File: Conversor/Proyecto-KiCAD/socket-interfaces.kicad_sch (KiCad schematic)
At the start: 24 parts, among them J7 DIMM100, P10 Header PWM, P11 Header ADC, P12 Header GPIO, P13 Header SD, P7 Header 7X2, P8 Header UART, P9 Header I2C, SW1 Switch, SW2 Switch, SW3 Switch, SW4 Switch

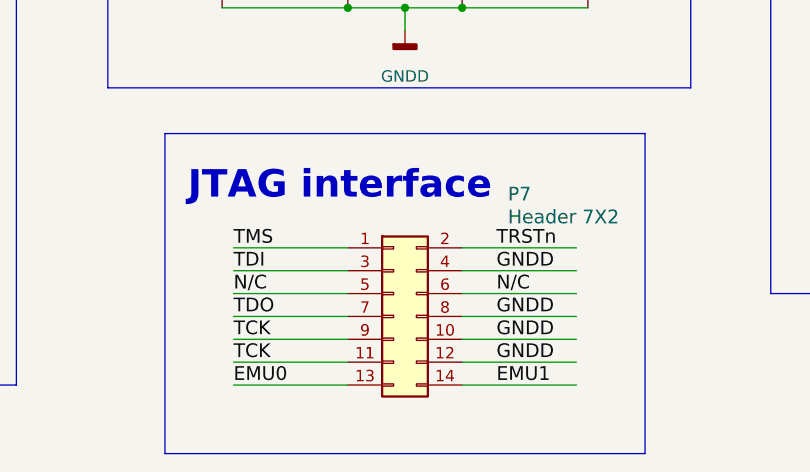
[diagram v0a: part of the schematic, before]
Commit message: Solucionar la union de las lineas de datos I2C
- Segun una evaluation board de Texas, si ya estan separadas las lineas
de I2C como en este caso, solo hay que agregar un adaptador de push-pull
a opne-drain a la salida del aislador
- Se mandó el mail a MayerPCB
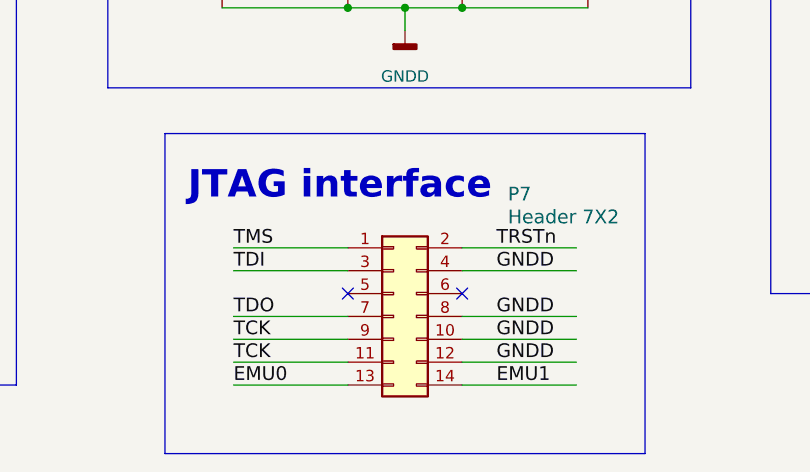
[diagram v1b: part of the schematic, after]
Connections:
- net N/C: no longer names the net of P7.6 (Pin_6)
- net N/C: no longer names the net of P7.5 (Pin_5)
- no-connect marks 15 -> 17
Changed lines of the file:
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@@
   (no_connect (at 35.56 29.21))
   (no_connect (at 60.96 34.29))
+  (no_connect (at 133.35 154.94))
+  (no_connect (at 120.65 154.94))
   (no_connect (at 60.96 67.31))
   (no_connect (at 60.96 31.75))
@@
     (stroke (width 0) (type default) (color 0 0 0 0))
   )
-  (wire (pts (xy 107.95 154.94) (xy 120.65 154.94))
-    (stroke (width 0) (type default) (color 0 0 0 0))
-  )
   (wire (pts (xy 25.4 74.93) (xy 35.56 74.93))
     (stroke (width 0) (type default) (color 0 0 0 0))
@@
   )
   (wire (pts (xy 120.65 90.17) (xy 120.65 93.98))
-    (stroke (width 0) (type default) (color 0 0 0 0))
-  )
-  (wire (pts (xy 146.05 154.94) (xy 133.35 154.94))
     (stroke (width 0) (type default) (color 0 0 0 0))
   )
@@
     (effects (font (size 1.27 1.27)) (justify left bottom))
   )
-  (label "N/C" (at 137.16 154.94 0)
-    (effects (font (size 1.524 1.524)) (justify left bottom))
-  )
   (label "GPIO-12" (at 25.4 110.49 0)
     (effects (font (size 1.524 1.524)) (justify left bottom))
@@
     (effects (font (size 1.524 1.524)) (justify left bottom))
   )
-  (label "N{slash}C" (at 107.95 154.94 0)
-    (effects (font (size 1.524 1.524)) (justify left bottom))
-  )

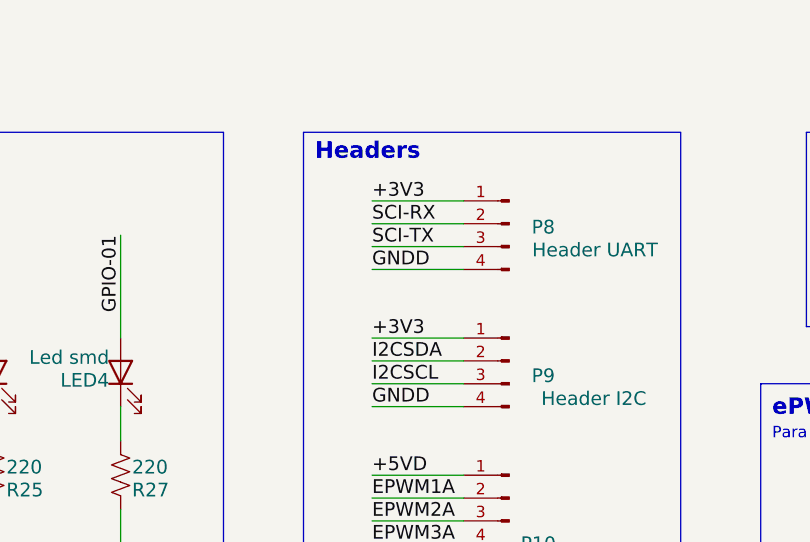
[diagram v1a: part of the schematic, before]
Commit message: Agregar resistencias de pull-up faltantes
- Agregar resistencias de pull-up a la salida de cada inversor del
74LS06
- Crear plano de U5V en la capa superior alrededor del FTDI
- Ponerle los valores a los componentes para poder generar correctamente
el BOM (Bill of Materials)
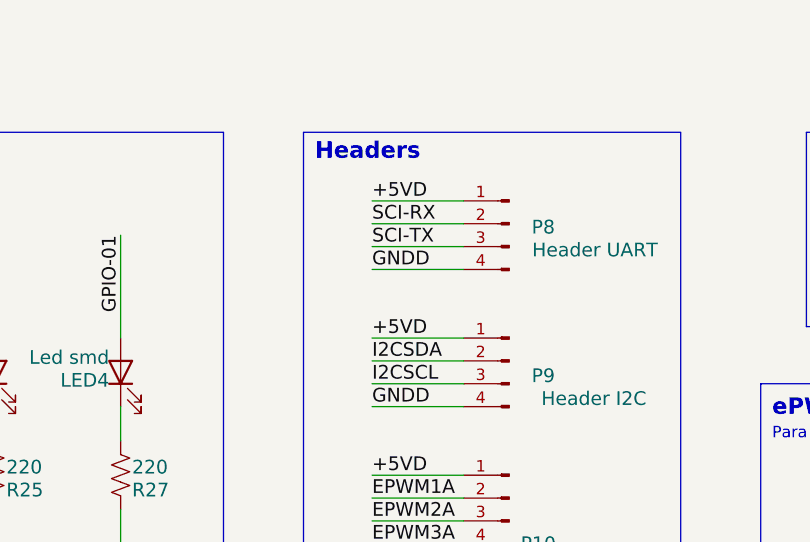
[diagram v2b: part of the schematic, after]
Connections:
- net +3V3: no longer P8.1 (Pin_1), P9.1 (Pin_1)
- net +5VD: now also P8.1 (Pin_1), P9.1 (Pin_1)
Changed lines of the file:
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@@
     (effects (font (size 1.524 1.524)) (justify left bottom))
   )
-  (label "+3V3" (at 175.26 35.56 0)
+  (label "+5VD" (at 175.26 35.56 0)
     (effects (font (size 1.524 1.524)) (justify left bottom))
   )
@@
     (effects (font (size 1.524 1.524)) (justify left bottom))
   )
-  (label "+3V3" (at 175.26 50.8 0)
+  (label "+5VD" (at 175.26 50.8 0)
     (effects (font (size 1.524 1.524)) (justify left bottom))
   )

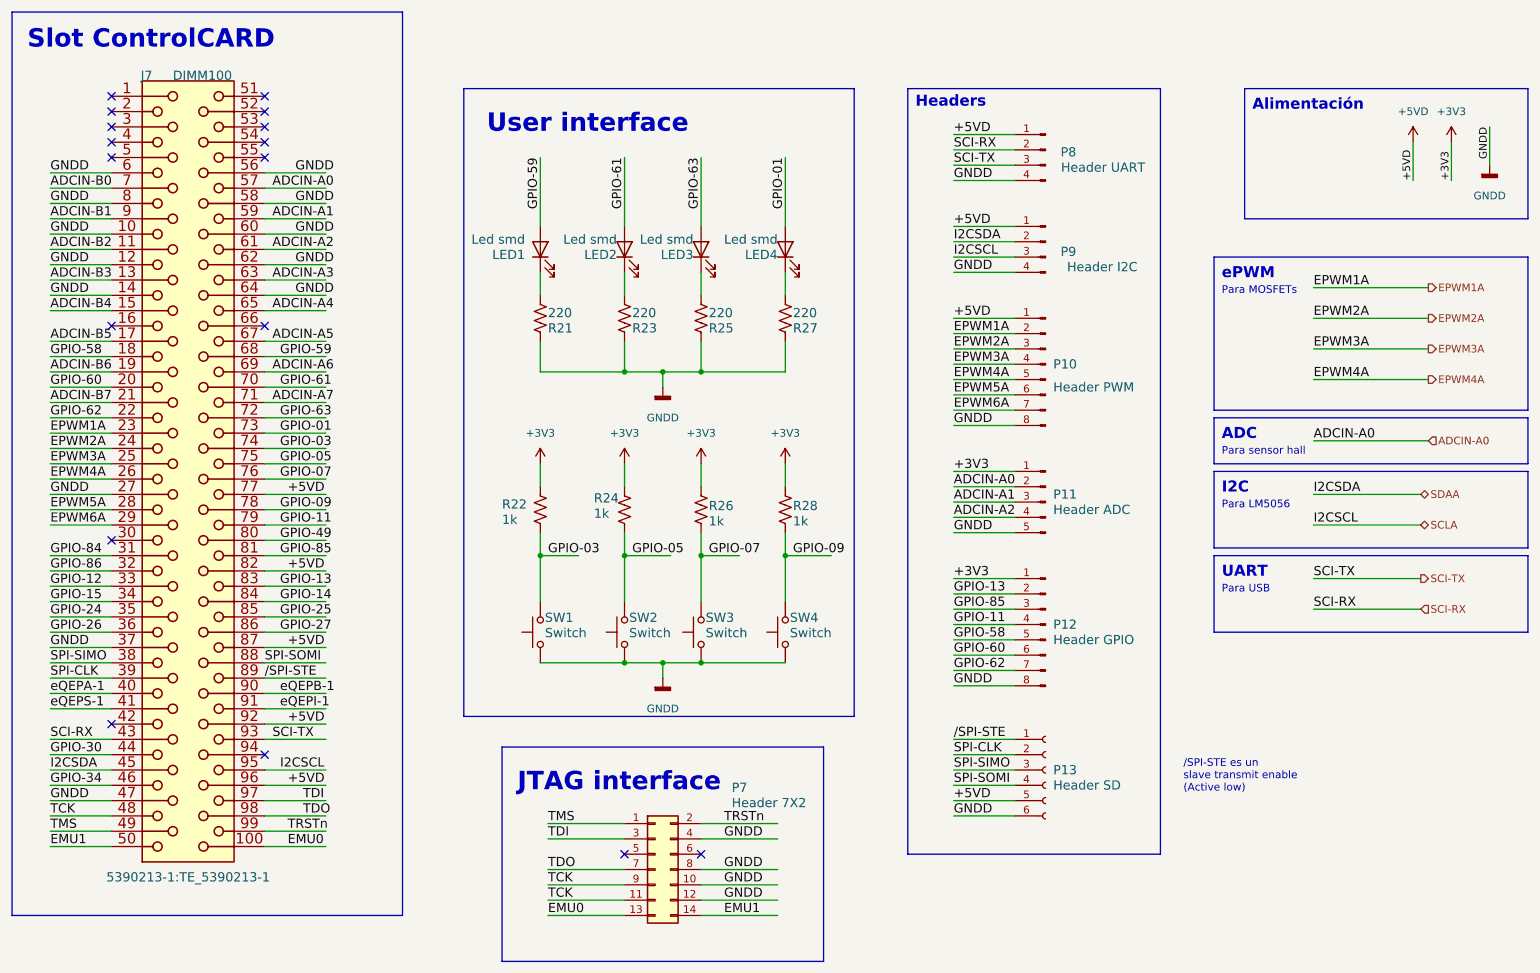
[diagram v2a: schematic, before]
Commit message: Eliminar resistencias de pull-up de SCL y SDAI
- Se pueden remover las Rpu del lado del sensor ya que las Rpu de esas
lineas estan del otro lado (la barrera de aislación proteje de daños).
La de SDAO tiene que quedar por la salida open-drain del LM5056.
- También cambiar las Rpu de 10k a 4k7, porque la capacidad del bus es
muy baja (un solo esclavo y pistas cortas). Así se disminuye es rise
time (Rpu*Cbus) a la mitad.
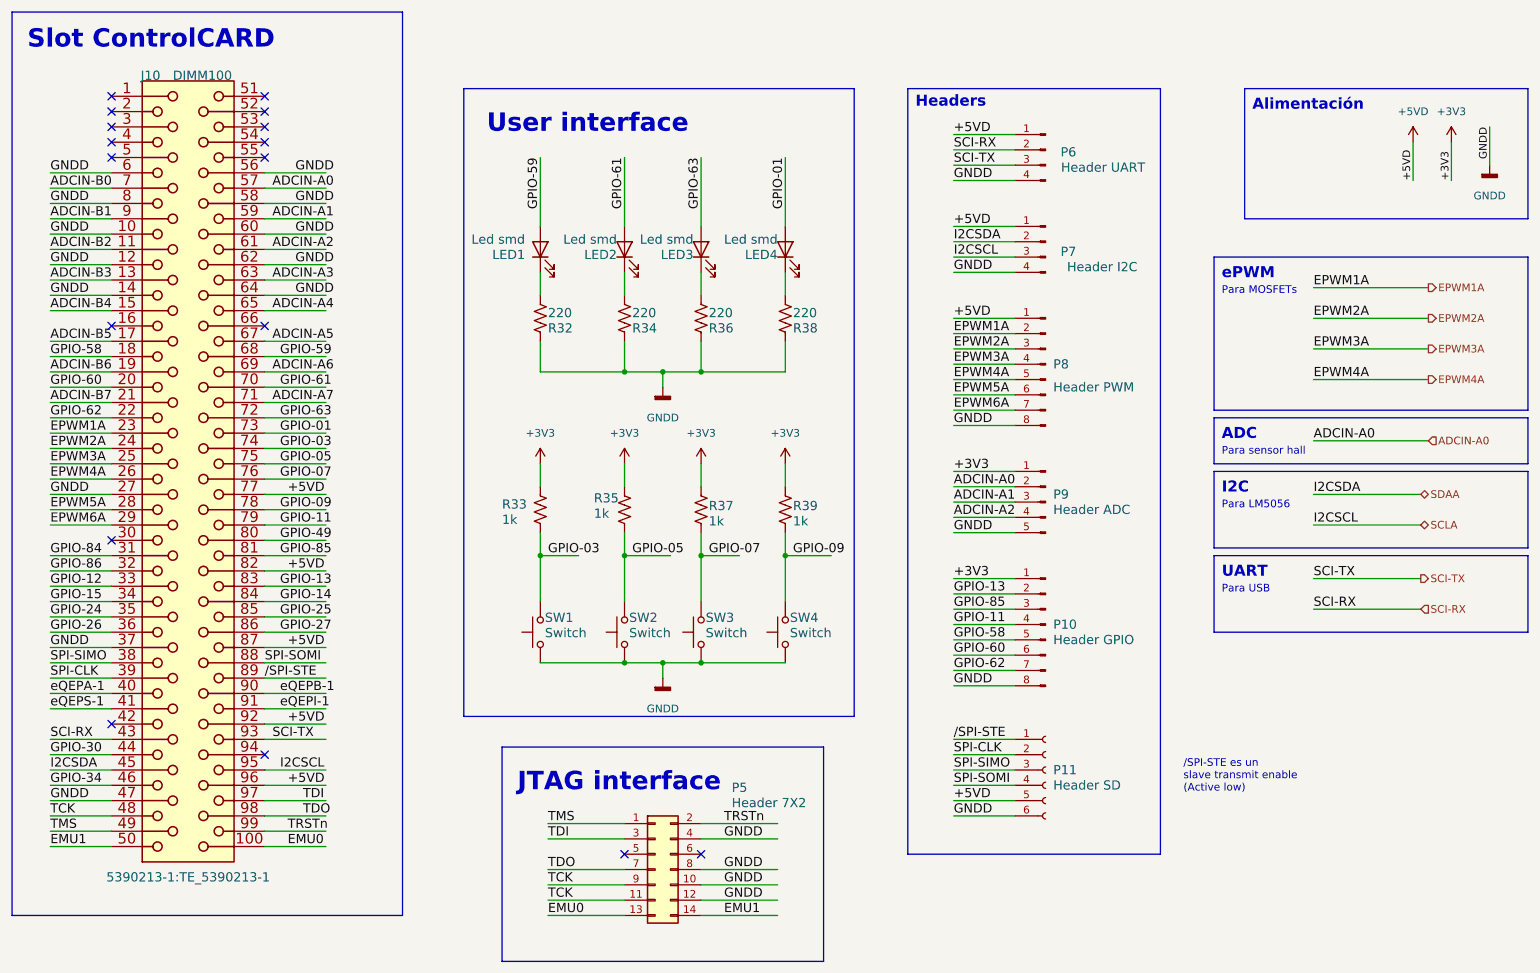
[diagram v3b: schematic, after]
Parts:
- renumbered J7 to J10, P12 to P10, P13 to P11, P7 to P5, P8 to P6, P9 to P7, P10 to P8, P11 to P9, R21 to R32, R22 to R33, R23 to R34, R24 to R35, R25 to R36, R26 to R37, R27 to R38, R28 to R39
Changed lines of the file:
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@@
   (symbol (lib_id "power:+3V3") (at 133.35 90.17 0) (unit 1)
     (in_bom yes) (on_board yes) (fields_autoplaced)
-    (property "Reference" "#PWR080" (id 0) (at 133.35 93.98 0)
+    (property "Reference" "#PWR088" (id 0) (at 133.35 93.98 0)
       (effects (font (size 1.27 1.27)) hide)
     )
@@
   (symbol (lib_id "Device:R_US") (at 133.35 97.79 180) (unit 1)
     (in_bom yes) (on_board yes)
-    (property "Reference" "R26" (id 0) (at 134.62 98.044 0)
+    (property "Reference" "R37" (id 0) (at 134.62 98.044 0)
       (effects (font (size 1.524 1.524)) (justify right top))
     )
@@
   (symbol (lib_id "power:+3V3") (at 120.65 90.17 0) (unit 1)
     (in_bom yes) (on_board yes) (fields_autoplaced)
-    (property "Reference" "#PWR077" (id 0) (at 120.65 93.98 0)
+    (property "Reference" "#PWR085" (id 0) (at 120.65 93.98 0)
       (effects (font (size 1.27 1.27)) hide)
     )
@@
   (symbol (lib_id "Connector:Conn_01x04_Male") (at 190.5 38.1 0) (mirror y) (unit 1)
     (in_bom yes) (on_board yes)
-    (property "Reference" "P8" (id 0) (at 195.58 39.37 0)
+    (property "Reference" "P6" (id 0) (at 195.58 39.37 0)
       (effects (font (size 1.524 1.524)) (justify left bottom))
     )
@@
   (symbol (lib_id "Device:R_US") (at 120.65 66.04 0) (unit 1)
     (in_bom yes) (on_board yes)
-    (property "Reference" "R23" (id 0) (at 121.92 68.58 0)
+    (property "Reference" "R34" (id 0) (at 121.92 68.58 0)
       (effects (font (size 1.524 1.524)) (justify left bottom))
     )
@@
   (symbol (lib_id "DIMM100:390213-1-") (at 55.88 26.67 270) (unit 1)
     (in_bom yes) (on_board yes)
-    (property "Reference" "J7" (id 0) (at 40.386 26.67 90)
+    (property "Reference" "J10" (id 0) (at 40.386 26.67 90)
       (effects (font (size 1.524 1.524)) (justify left bottom))
     )
@@
   (symbol (lib_id "Connector_Generic:Conn_02x07_Odd_Even") (at 125.73 157.48 0) (unit 1)
     (in_bom yes) (on_board yes)
-    (property "Reference" "P7" (id 0) (at 138.43 144.78 0)
+    (property "Reference" "P5" (id 0) (at 138.43 144.78 0)
       (effects (font (size 1.524 1.524)) (justify left bottom))
     )
@@
   (symbol (lib_id "power:+3V3") (at 147.32 90.17 0) (unit 1)
     (in_bom yes) (on_board yes) (fields_autoplaced)
-    (property "Reference" "#PWR081" (id 0) (at 147.32 93.98 0)
+    (property "Reference" "#PWR089" (id 0) (at 147.32 93.98 0)
       (effects (font (size 1.27 1.27)) hide)
     )
@@
   (symbol (lib_id "Device:R_US") (at 106.68 66.04 0) (unit 1)
     (in_bom yes) (on_board yes)
-    (property "Reference" "R21" (id 0) (at 107.95 68.58 0)
+    (property "Reference" "R32" (id 0) (at 107.95 68.58 0)
       (effects (font (size 1.524 1.524)) (justify left bottom))
     )
@@
   (symbol (lib_id "Connector:Conn_01x04_Male") (at 190.5 53.34 0) (mirror y) (unit 1)
     (in_bom yes) (on_board yes)
-    (property "Reference" "P9" (id 0) (at 195.58 55.88 0)
+    (property "Reference" "P7" (id 0) (at 195.58 55.88 0)
       (effects (font (size 1.524 1.524)) (justify left bottom))
     )
@@
   (symbol (lib_id "Device:R_US") (at 147.32 66.04 0) (unit 1)
     (in_bom yes) (on_board yes)
-    (property "Reference" "R27" (id 0) (at 148.59 68.58 0)
+    (property "Reference" "R38" (id 0) (at 148.59 68.58 0)
       (effects (font (size 1.524 1.524)) (justify left bottom))
     )
@@
   (symbol (lib_id "Connector:Conn_01x06_Female") (at 190.5 140.97 0) (unit 1)
     (in_bom yes) (on_board yes)
-    (property "Reference" "P13" (id 0) (at 191.77 140.97 0)
+    (property "Reference" "P11" (id 0) (at 191.77 140.97 0)
       (effects (font (size 1.524 1.524)) (justify left))
     )
@@
   (symbol (lib_id "power:GNDD") (at 127 77.47 0) (unit 1)
     (in_bom yes) (on_board yes) (fields_autoplaced)
-    (property "Reference" "#PWR078" (id 0) (at 127 83.82 0)
+    (property "Reference" "#PWR086" (id 0) (at 127 83.82 0)
       (effects (font (size 1.27 1.27)) hide)
     )
@@
   (symbol (lib_id "Device:R_US") (at 120.65 97.79 180) (unit 1)
     (in_bom yes) (on_board yes)
-    (property "Reference" "R24" (id 0) (at 115.57 96.774 0)
+    (property "Reference" "R35" (id 0) (at 115.57 96.774 0)
       (effects (font (size 1.524 1.524)) (justify right top))
     )
@@
   (symbol (lib_id "Connector:Conn_01x05_Male") (at 190.5 96.52 0) (mirror y) (unit 1)
     (in_bom yes) (on_board yes)
-    (property "Reference" "P11" (id 0) (at 191.77 95.25 0)
+    (property "Reference" "P9" (id 0) (at 191.77 95.25 0)
       (effects (font (size 1.524 1.524)) (justify right))
     )
@@
   (symbol (lib_id "Device:R_US") (at 133.35 66.04 0) (unit 1)
     (in_bom yes) (on_board yes)
-    (property "Reference" "R25" (id 0) (at 134.62 68.58 0)
+    (property "Reference" "R36" (id 0) (at 134.62 68.58 0)
       (effects (font (size 1.524 1.524)) (justify left bottom))
     )
@@
   (symbol (lib_id "Connector:Conn_01x08_Male") (at 190.5 116.84 0) (mirror y) (unit 1)
     (in_bom yes) (on_board yes)
-    (property "Reference" "P12" (id 0) (at 191.77 116.84 0)
+    (property "Reference" "P10" (id 0) (at 191.77 116.84 0)
       (effects (font (size 1.524 1.524)) (justify right))
     )
@@
   (symbol (lib_id "power:+5VD") (at 251.46 36.83 0) (unit 1)
     (in_bom yes) (on_board yes) (fields_autoplaced)
-    (property "Reference" "#PWR082" (id 0) (at 251.46 40.64 0)
+    (property "Reference" "#PWR090" (id 0) (at 251.46 40.64 0)
       (effects (font (size 1.27 1.27)) hide)
     )
@@
   (symbol (lib_id "power:GNDD") (at 264.16 40.64 0) (unit 1)
     (in_bom yes) (on_board yes) (fields_autoplaced)
-    (property "Reference" "#PWR084" (id 0) (at 264.16 46.99 0)
+    (property "Reference" "#PWR092" (id 0) (at 264.16 46.99 0)
       (effects (font (size 1.27 1.27)) hide)
     )
@@
   (symbol (lib_id "power:+3V3") (at 106.68 90.17 0) (unit 1)
     (in_bom yes) (on_board yes) (fields_autoplaced)
-    (property "Reference" "#PWR076" (id 0) (at 106.68 93.98 0)
+    (property "Reference" "#PWR084" (id 0) (at 106.68 93.98 0)
       (effects (font (size 1.27 1.27)) hide)
     )
@@
   (symbol (lib_id "power:+3V3") (at 257.81 36.83 0) (unit 1)
     (in_bom yes) (on_board yes) (fields_autoplaced)
-    (property "Reference" "#PWR083" (id 0) (at 257.81 40.64 0)
+    (property "Reference" "#PWR091" (id 0) (at 257.81 40.64 0)
       (effects (font (size 1.27 1.27)) hide)
     )
@@
   (symbol (lib_id "Connector:Conn_01x08_Male") (at 190.5 73.66 0) (mirror y) (unit 1)
     (in_bom yes) (on_board yes) (fields_autoplaced)
-    (property "Reference" "P10" (id 0) (at 191.77 73.66 0)
+    (property "Reference" "P8" (id 0) (at 191.77 73.66 0)
       (effects (font (size 1.524 1.524)) (justify right))
     )
@@
   (symbol (lib_id "Device:R_US") (at 147.32 97.79 180) (unit 1)
     (in_bom yes) (on_board yes)
-    (property "Reference" "R28" (id 0) (at 148.59 98.044 0)
+    (property "Reference" "R39" (id 0) (at 148.59 98.044 0)
       (effects (font (size 1.524 1.524)) (justify right top))
     )
@@
   (symbol (lib_id "Device:R_US") (at 106.68 97.79 180) (unit 1)
     (in_bom yes) (on_board yes)
-    (property "Reference" "R22" (id 0) (at 100.33 97.79 0)
+    (property "Reference" "R33" (id 0) (at 100.33 97.79 0)
       (effects (font (size 1.524 1.524)) (justify right top))
     )
@@
   (symbol (lib_id "power:GNDD") (at 127 125.73 0) (unit 1)
     (in_bom yes) (on_board yes) (fields_autoplaced)
-    (property "Reference" "#PWR079" (id 0) (at 127 132.08 0)
-      (effects (font (size 1.27 1.27)) hide)
-    )
+    (property "Reference" "#PWR087" (id 0) (at 127 132.08 0)
+      (effects (font (size 1.27 1.27)) hide)
+    )
